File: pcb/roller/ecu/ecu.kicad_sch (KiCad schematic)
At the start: 0 parts

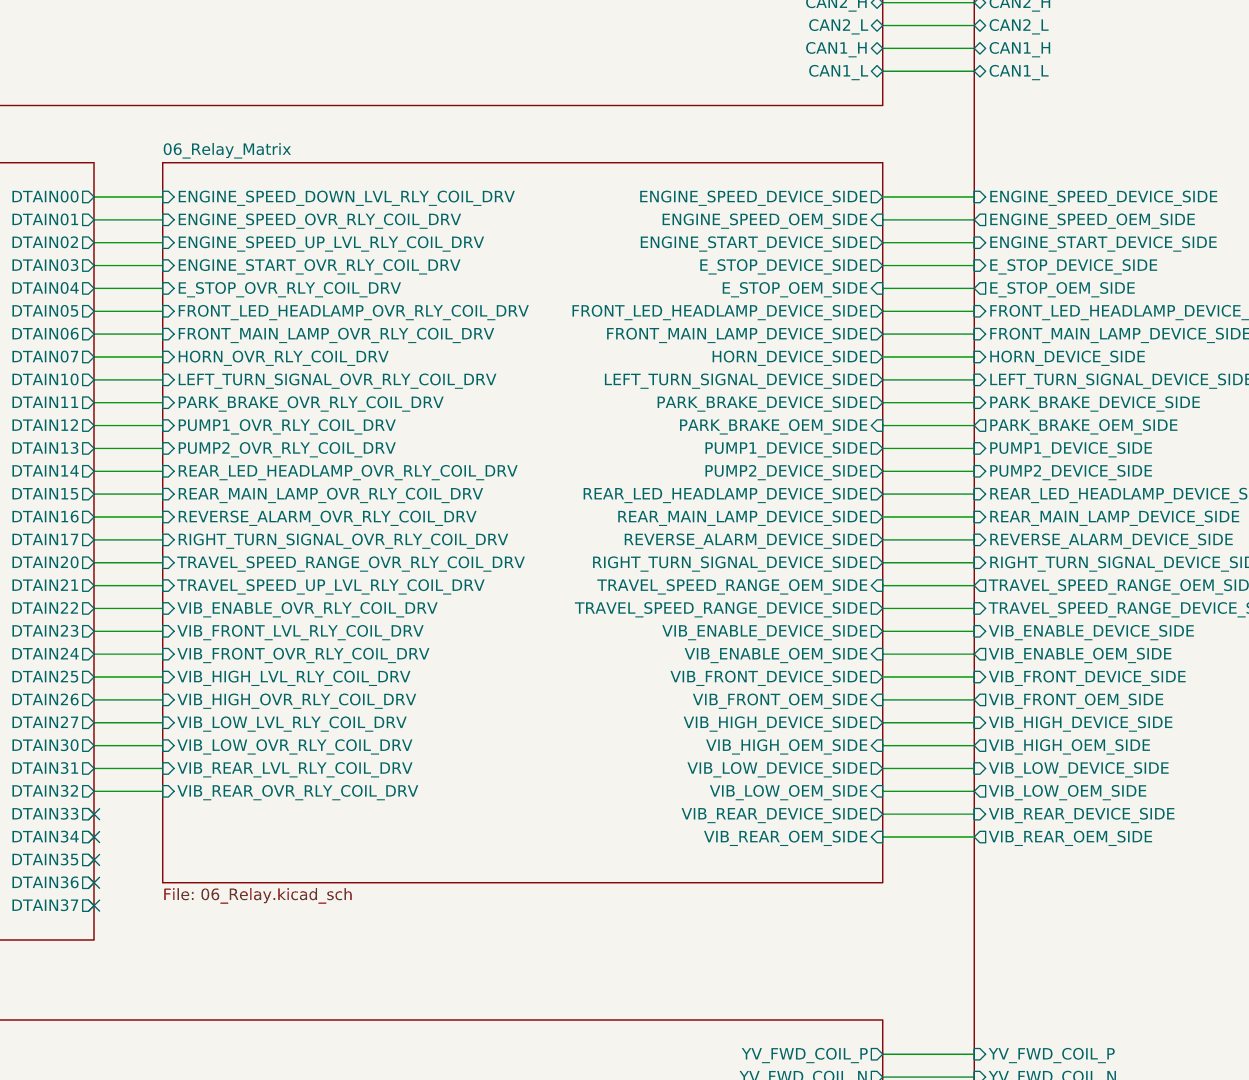
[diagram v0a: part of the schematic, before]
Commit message: Add ESTOP_NC pin and wire connections in ECU schematic; update designators in PCB project
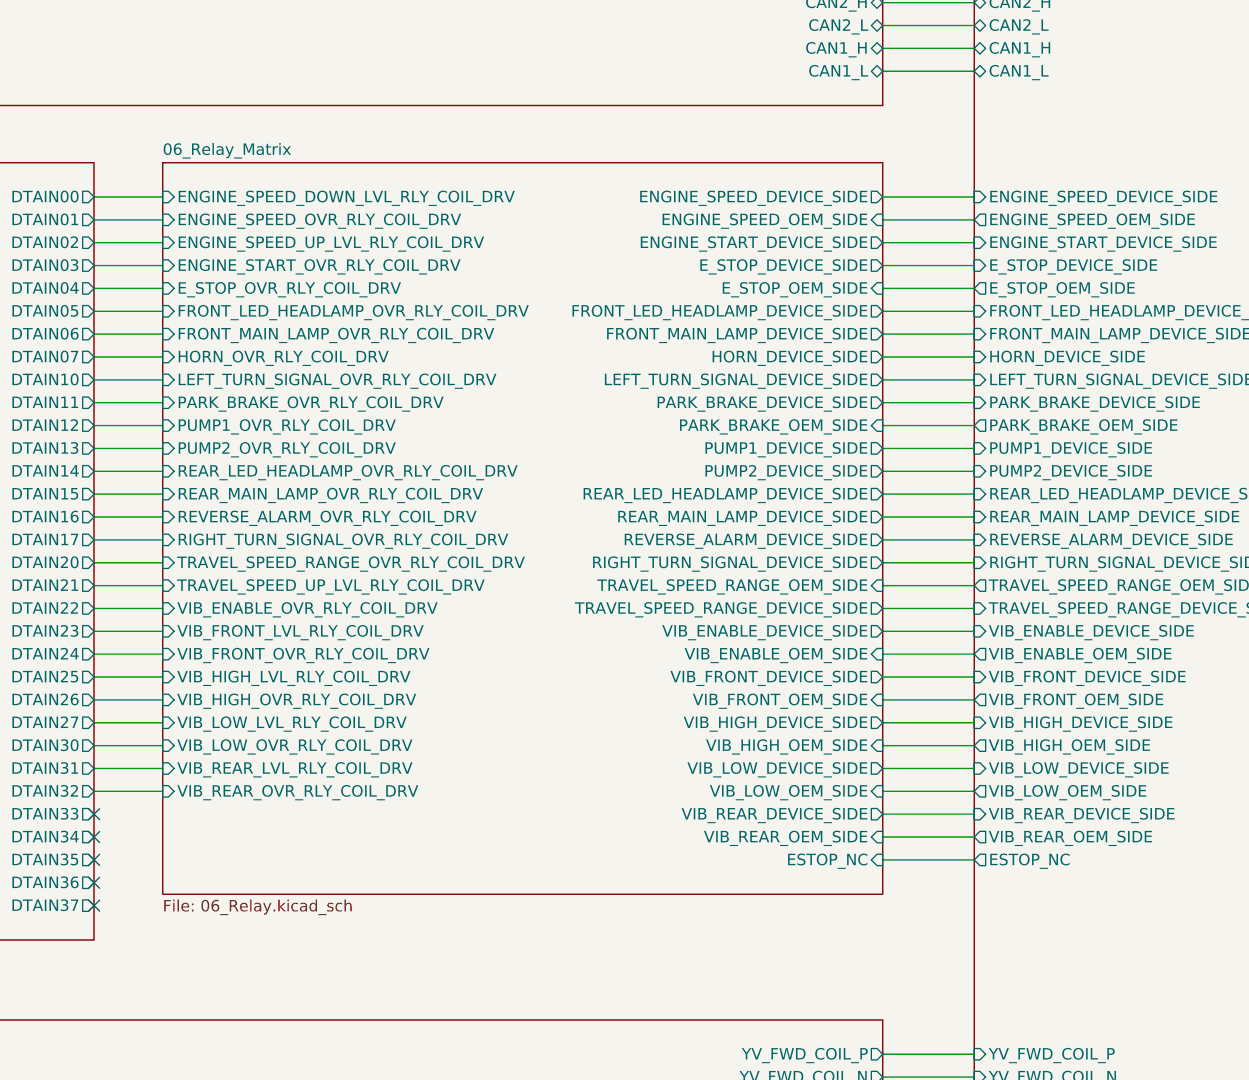
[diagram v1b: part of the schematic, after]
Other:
- sheet 06_Relay_Matrix ports: added ESTOP_NC; removed none
- sheet 09_Connectors ports: added ESTOP_NC; removed none
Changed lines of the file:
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@@
+	(wire
+		(pts
+			(xy 267.97 162.56) (xy 278.13 162.56)
+		)
+		(stroke
+			(width 0)
+			(type default)
+		)
+	)
 	(wire
 		(pts
@@
 			)
 		)
+		(pin "ESTOP_NC" output
+			(at 278.13 162.56 180)
+			(effects
+				(font
+					(size 1.27 1.27)
+				)
+				(justify left)
+			)
+		)
 		(instances
 			(project "ecu"
@@
 	(sheet
 		(at 187.96 85.09)
-		(size 80.01 80.01)
+		(size 80.01 81.28)
 		(exclude_from_sim no)
 		(in_bom yes)
@@
 		)
 		(property "Sheetfile" "06_Relay.kicad_sch"
-			(at 187.96 165.6846 0)
+			(at 187.96 166.9546 0)
 			(show_name no)
 			(do_not_autoplace no)
@@
 			(effects
 				(font
+					(size 1.27 1.27)
+				)
+				(justify right)
+			)
+		)
+		(pin "ESTOP_NC" input
+			(at 267.97 162.56 0)
+			(effects
+				(font

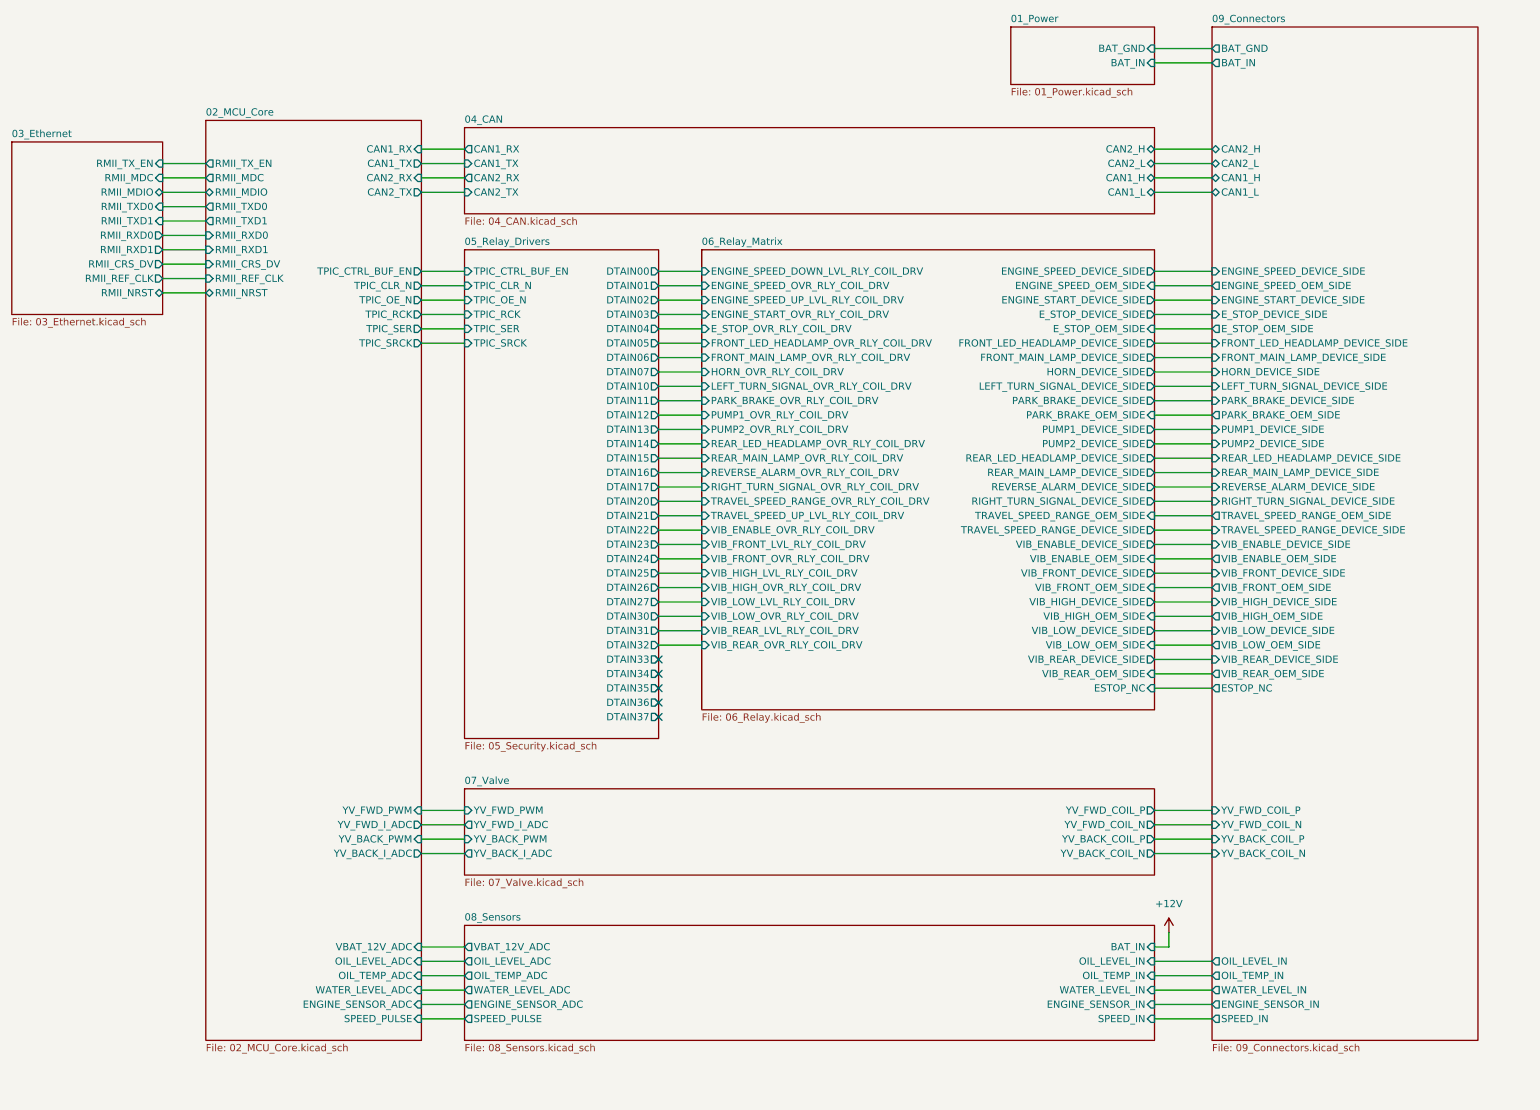
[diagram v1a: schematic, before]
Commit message: Refactor ECU schematic and project files
- Updated used designators in ecu.kicad_pro to reflect current components.
- Adjusted wire connections in ecu.kicad_sch for better layout and clarity.
- Added new wires and labels for ESTOP functionality.
- Modified pin placements and sizes for improved organization in the schematic.
- Ensured all changes maintain compatibility with existing design specifications.
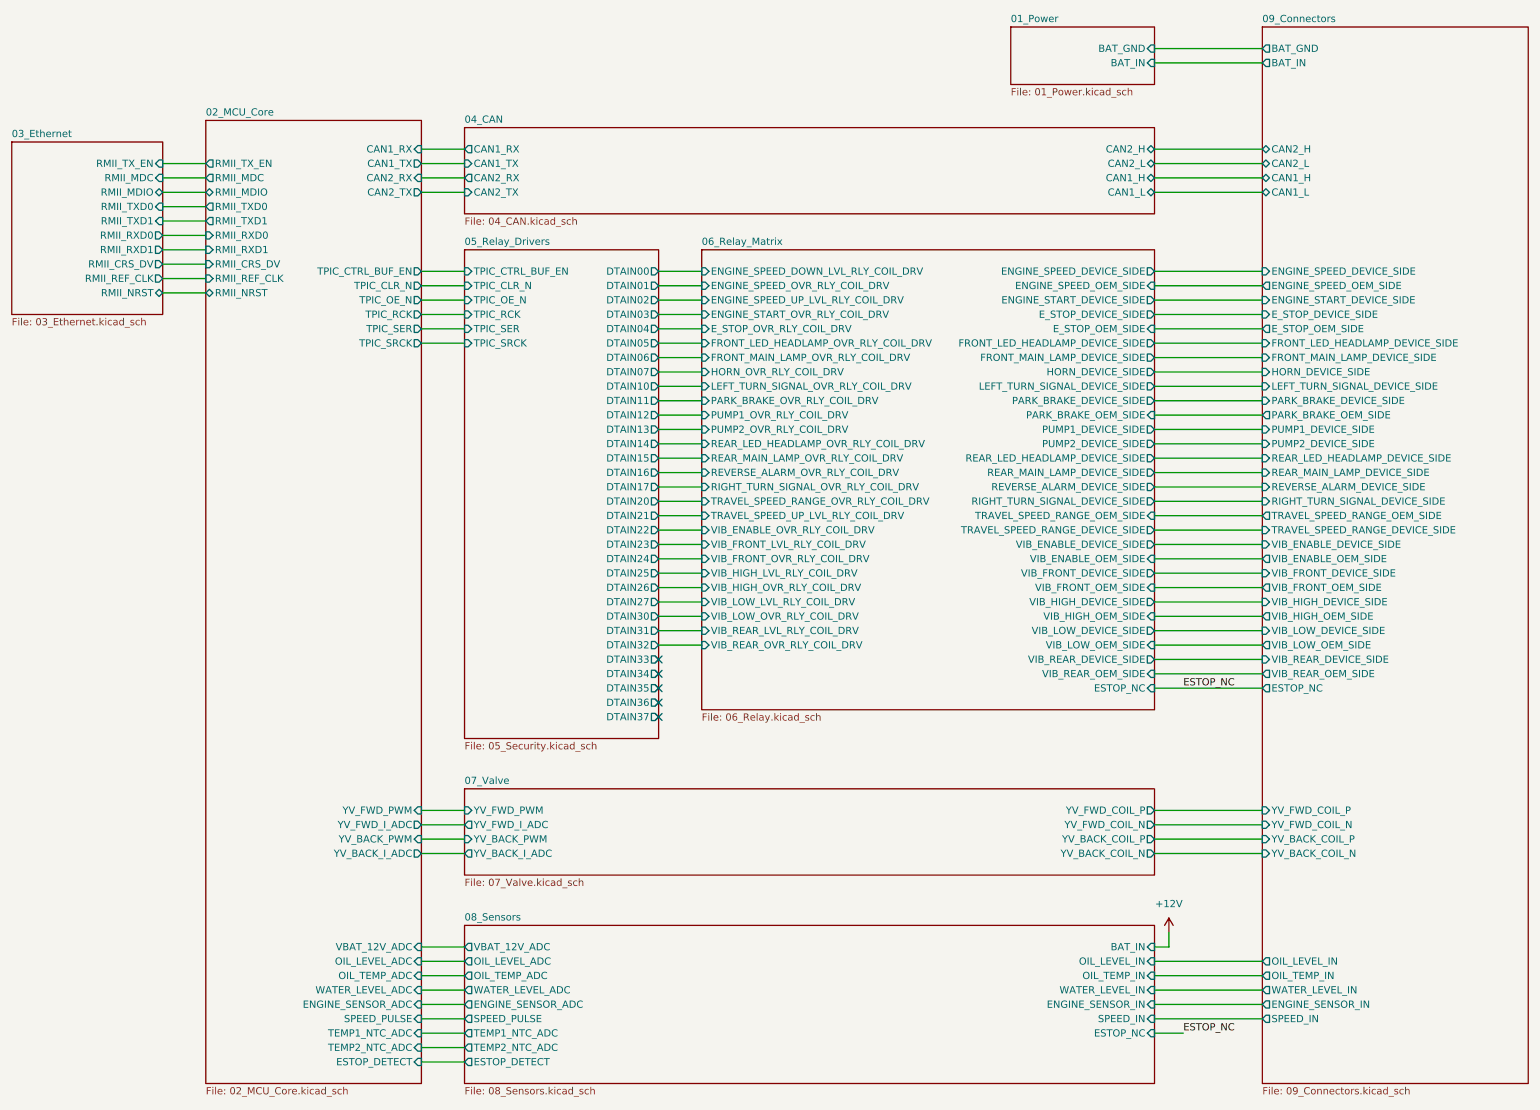
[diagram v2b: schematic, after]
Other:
- sheet 02_MCU_Core ports: added ESTOP_DETECT, TEMP1_NTC_ADC, TEMP2_NTC_ADC; removed none
- sheet 08_Sensors ports: added ESTOP_DETECT, ESTOP_NC, TEMP1_NTC_ADC, TEMP2_NTC_ADC; removed none

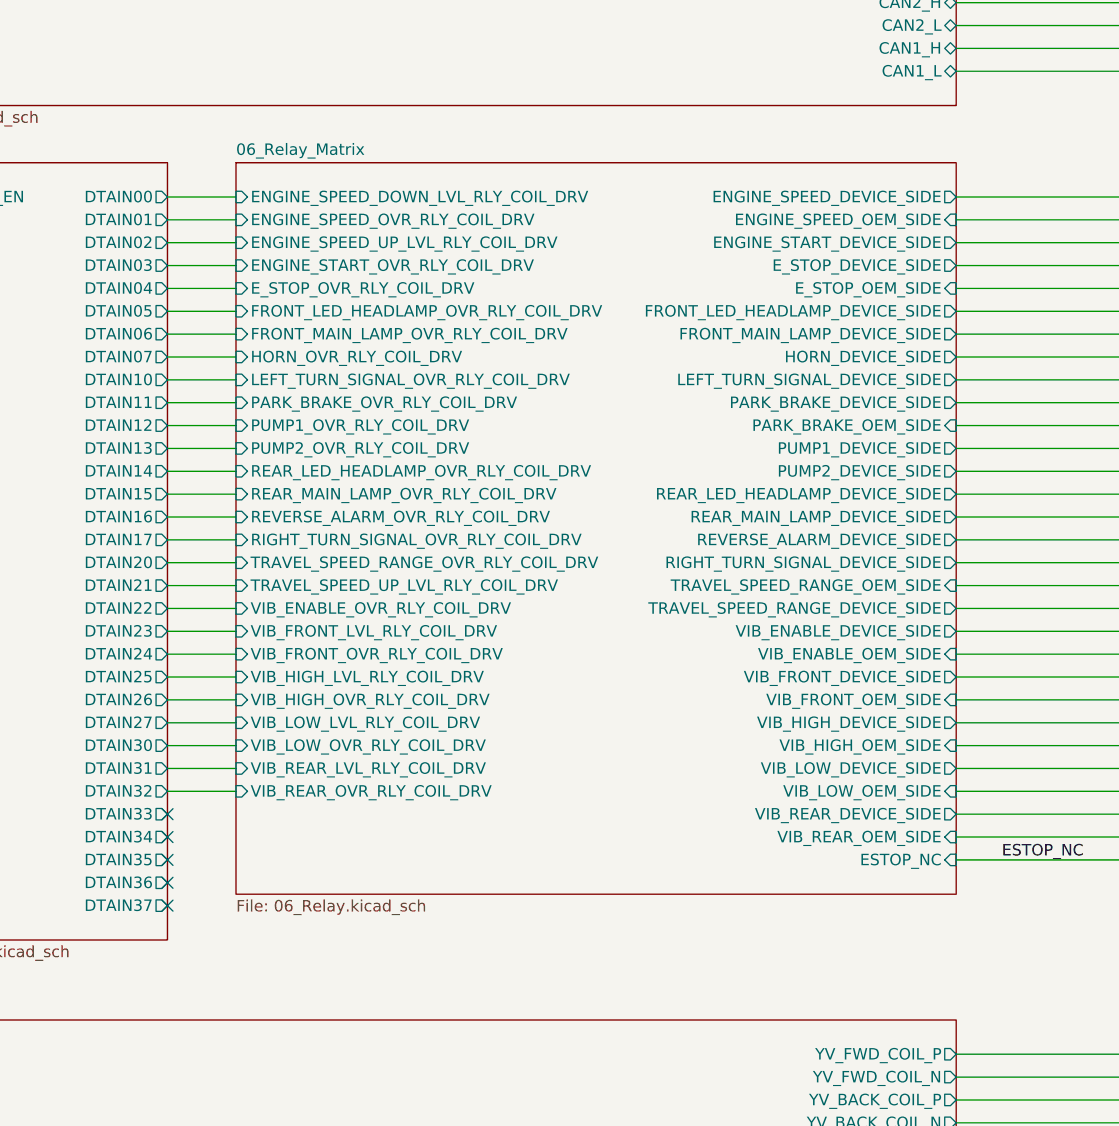
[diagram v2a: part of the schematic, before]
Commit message: Refactor ECU schematic: Adjust wire connections and update no_connect points
- Modified coordinates for several no_connect points to improve layout clarity.
- Adjusted wire connections to reflect updated schematic design.
- Removed redundant wire segments and ensured UUIDs are consistent with changes.
- Enhanced overall readability and organization of the schematic for better maintenance.
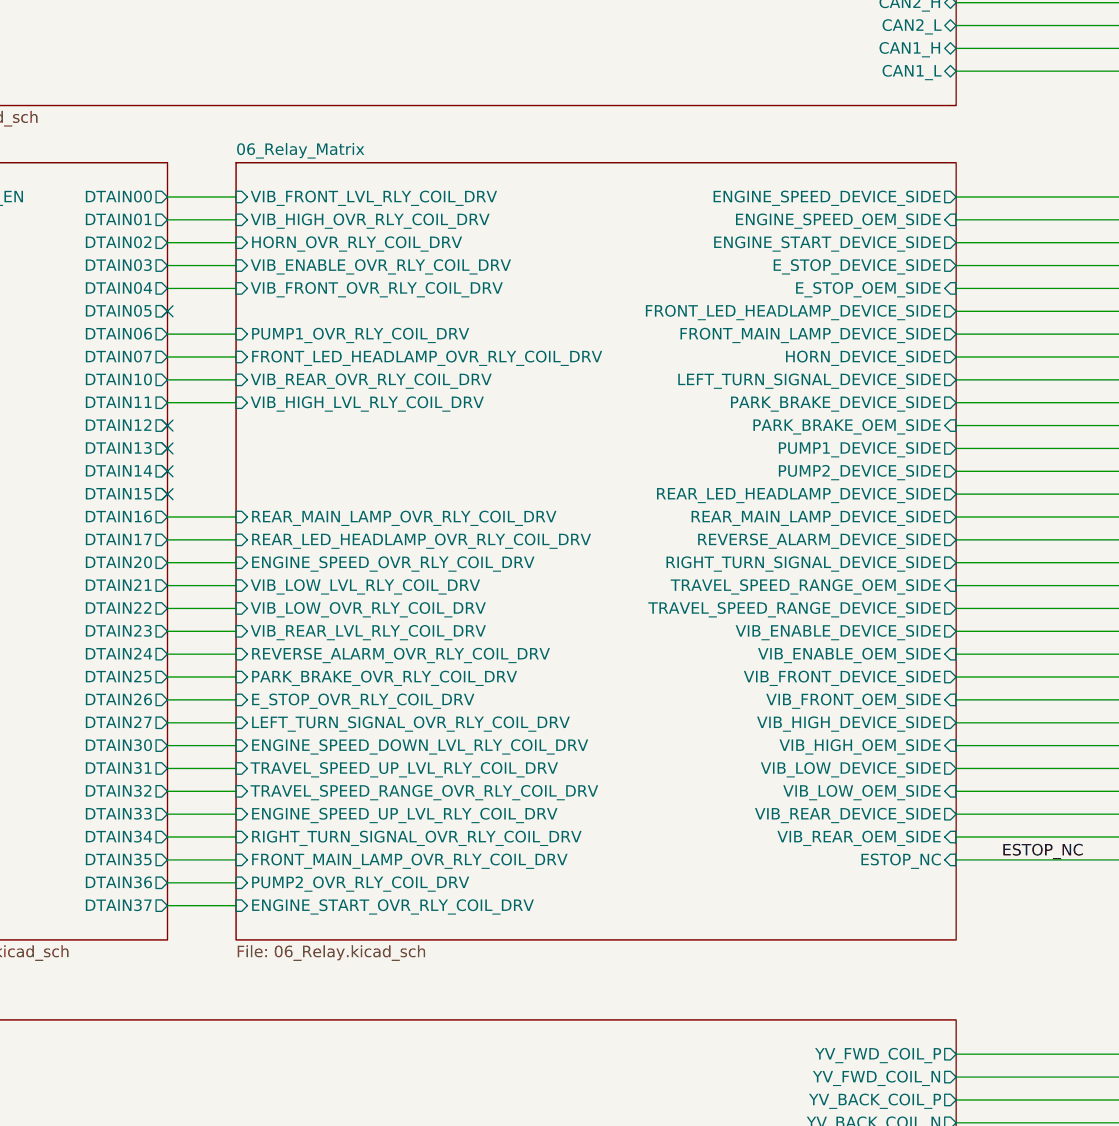
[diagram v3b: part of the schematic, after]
